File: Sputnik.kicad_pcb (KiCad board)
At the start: 4 copper layers, 130 x 65 mm, 179 parts, among them IC1 EP4CE10F17, J1 Pinheader_2x5_TH_WALL, P1 USB_A, U1 SN74LVC2T45, U10 SN74LVC8T245, U11 SN74LVC8T245, U12 SN74LVC8T245, U13 SN74LVC8T245, U14 SN74LVC8T245, U15 SN74LVC8T245, U16 SN74LVC2T45, U17 SN74LVC2T45, U18 SN74LVC2T45, U19 SN74LVC1G07DCK, U2 SN74LVC2T45, U20 SN74LVC2T45, U21 EPCS4, U22 W9751G6KB, U23 FT313HL-LQFP64-0.5, U24 TLV62569P, U25 TPS2024D, U3 SN74LVC1G07DCK, U4 SN74LVC2T45, U5 DM9000B, U6 93LC46, U7 74LVC2G07, U8 Pulse-J00-0045NL, U9 SN74LVC8T245, X2 Zorro_Connector, Y1 25MHz, Y2 12MHz

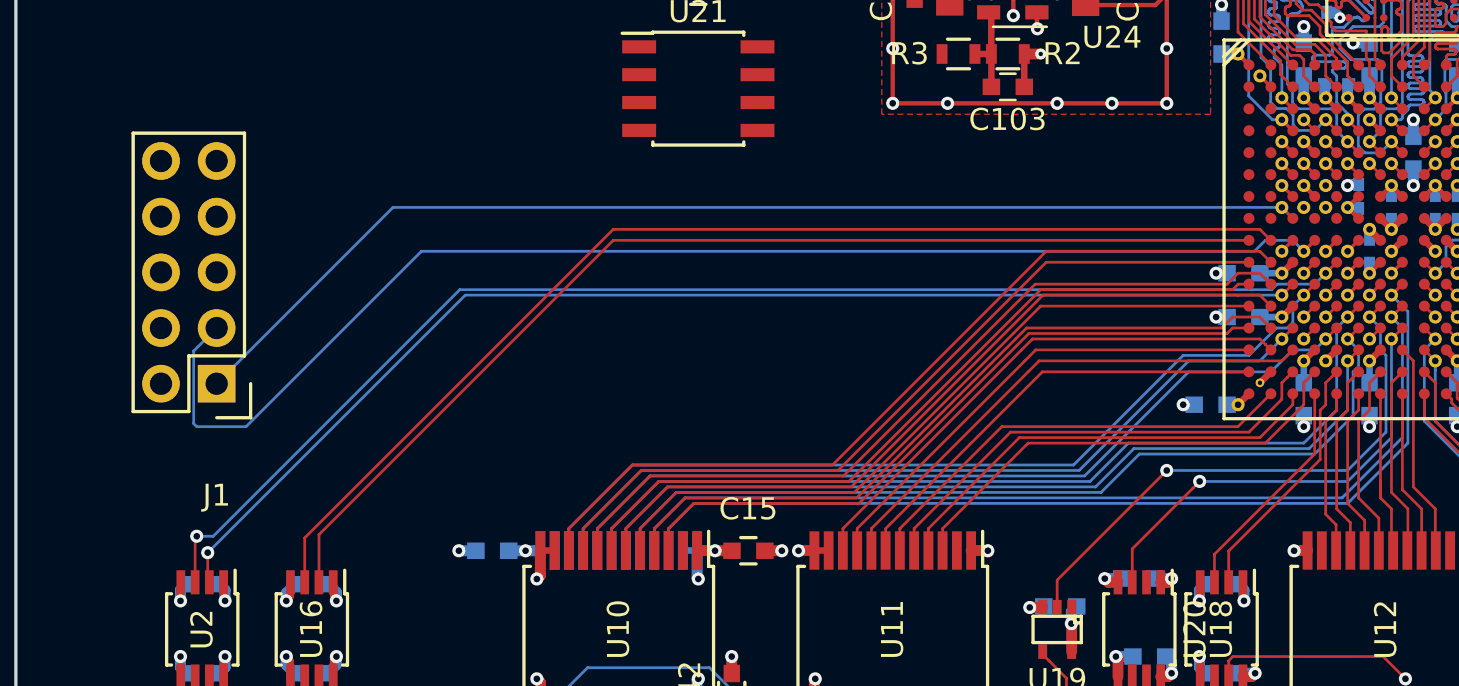
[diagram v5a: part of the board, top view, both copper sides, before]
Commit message: PCB rework, JTAG connector moved, VREF routed
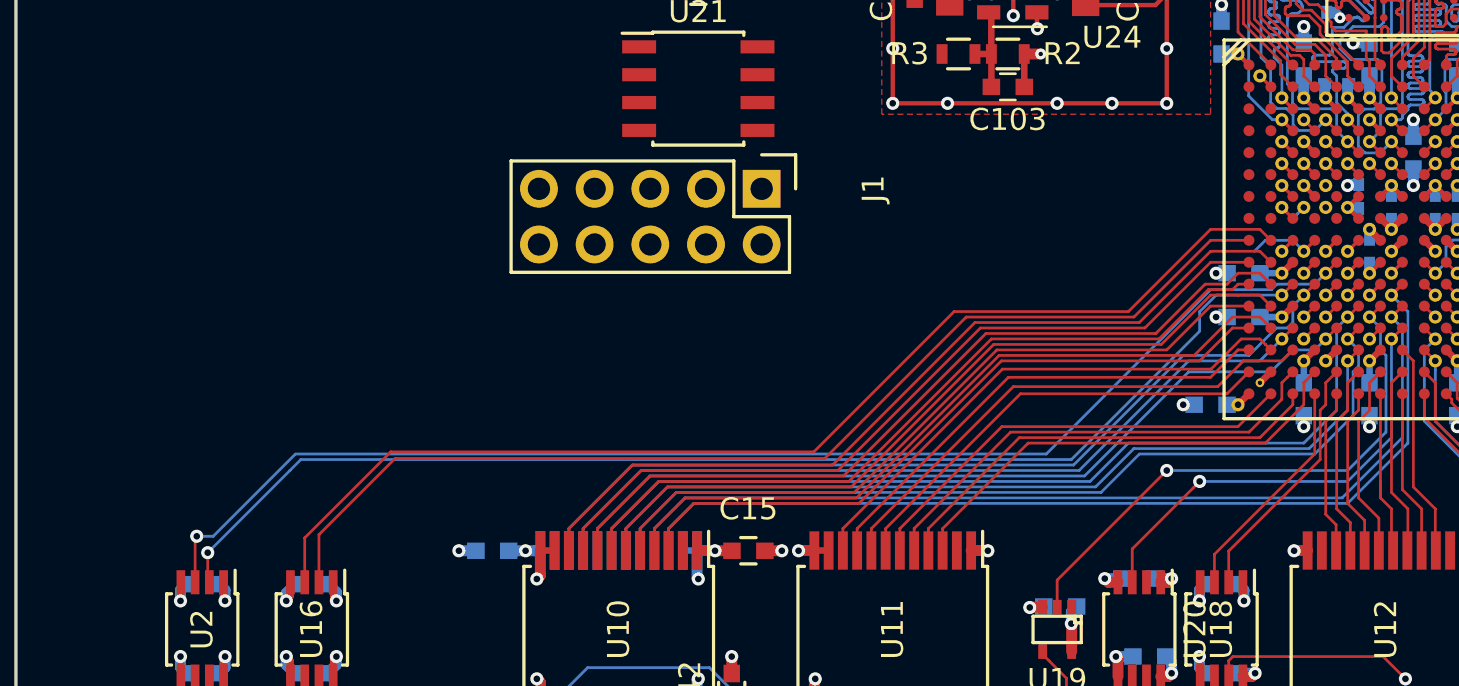
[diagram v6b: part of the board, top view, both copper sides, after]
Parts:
- moved J1 26.4 mm to (154.0, 41.4), turned to 270 degrees
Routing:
- net /fpga/TDO: track 59.9 -> 3.37 mm
- net /fpga/TCK: track 52.6 -> 0.71 mm
- net /RAM/VREF: track 20.4 -> 26.6 mm
- net (no net): track 0.00 -> 1.25 mm, vias 0 -> 4
- net +5VDC: track 117.7 -> 116.5 mm, vias 25 -> 21
- net /fpga/TDI: track 0.00 -> 0.69 mm
- net /Zorro/nIORST: track 56.0 -> 56.5 mm

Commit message: Up
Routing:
- net /fpga/TDO: track 3.37 -> 15.7 mm
- net /fpga/TMS: track 0.71 -> 9.27 mm
- net /fpga/TDI: track 0.69 -> 7.96 mm
- net /fpga/TCK: track 0.71 -> 7.27 mm
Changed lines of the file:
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@@
     (thickness 1.6)
     (drawings 9)
-    (tracks 7427)
+    (tracks 7436)
     (zones 0)
     (modules 179)
@@
   (segment (start 178.2509 40.75064) (end 178.25064 40.75064) (width 0.15) (layer F.Cu) (net 148))
   (segment (start 178.25064 40.75064) (end 177.75 40.25) (width 0.15) (layer F.Cu) (net 148))
+  (segment (start 177 43) (end 171.5 43) (width 0.125) (layer B.Cu) (net 150))
+  (segment (start 177.450001 42.549999) (end 177 43) (width 0.125) (layer B.Cu) (net 150))
+  (segment (start 177.75 42.25) (end 177.450001 42.549999) (width 0.125) (layer B.Cu) (net 150))
   (segment (start 178.2509 42.74962) (end 178.24962 42.74962) (width 0.15) (layer F.Cu) (net 150))
   (segment (start 178.24962 42.74962) (end 177.75 42.25) (width 0.15) (layer F.Cu) (net 150))
-  (segment (start 178.450001 42.549999) (end 178.262499 42.737501) (width 0.125) (layer B.Cu) (net 151))
-  (segment (start 178.75 42.25) (end 178.450001 42.549999) (width 0.125) (layer B.Cu) (net 151))
+  (segment (start 178.25 43.25) (end 171.5 43.25) (width 0.125) (layer B.Cu) (net 151))
+  (segment (start 178.75 42.75) (end 178.25 43.25) (width 0.125) (layer B.Cu) (net 151))
+  (segment (start 178.75 42.25) (end 178.75 42.75) (width 0.125) (layer B.Cu) (net 151))
+  (segment (start 178.25 43.75) (end 171.5 43.75) (width 0.125) (layer B.Cu) (net 152))
   (segment (start 178.75 44.25) (end 178.25 43.75) (width 0.125) (layer B.Cu) (net 152))
-  (segment (start 178.25 43.75) (end 177 43.75) (width 0.125) (layer B.Cu) (net 152))
-  (segment (start 177 43.75) (end 176.5 44.25) (width 0.125) (layer B.Cu) (net 152))
+  (segment (start 177.087501 44.5) (end 171.5 44.5) (width 0.125) (layer B.Cu) (net 152))
+  (segment (start 178.75 44.25) (end 178.25 44.75) (width 0.125) (layer B.Cu) (net 152))
+  (segment (start 178.25 44.75) (end 177.337501 44.75) (width 0.125) (layer B.Cu) (net 152))
+  (segment (start 177.337501 44.75) (end 177.087501 44.5) (width 0.125) (layer B.Cu) (net 152))
   (segment (start 179.24912 43.75038) (end 179.24912 43.75088) (width 0.15) (layer F.Cu) (net 152))
   (segment (start 179.24912 43.75088) (end 178.75 44.25) (width 0.15) (layer F.Cu) (net 152))
@@
   (segment (start 179.24912 53.50088) (end 179.24912 52.75088) (width 0.125) (layer F.Cu) (net 175))
   (segment (start 179.24912 52.75088) (end 179.24912 50.75062) (width 0.125) (layer F.Cu) (net 175))
+  (segment (start 179 43.5) (end 171.5 43.5) (width 0.125) (layer B.Cu) (net 177))
+  (segment (start 179.75 44.25) (end 179 43.5) (width 0.125) (layer B.Cu) (net 177))
   (segment (start 179.75 44.25) (end 179.75026 44.25) (width 0.15) (layer F.Cu) (net 177))
   (segment (start 179.75026 44.25) (end 180.24988 43.75038) (width 0.15) (layer F.Cu) (net 177))
@@
     (polygon
       (pts
-        (xy 182.25 41.75) (xy 182.25 40.5) (xy 186.25 40.5) (xy 186.25 43.75) (xy 184.5 43.75)
-        (xy 183.75 44.5) (xy 183.75 46) (xy 180 46) (xy 180 43.75) (xy 168 43.75)
-        (xy 168 42.75) (xy 180 42.75) (xy 180 41.75)
+        (xy 180.25 40.5) (xy 182.25 40.5) (xy 186.25 40.5) (xy 186.25 43.75) (xy 184.5 43.75)
+        (xy 183.75 44.5) (xy 183.75 45.75) (xy 180 45.75) (xy 180 43.75) (xy 168 43.75)
+        (xy 168 42.75) (xy 168 40.5) (xy 178.25 40.5)
       )
     )

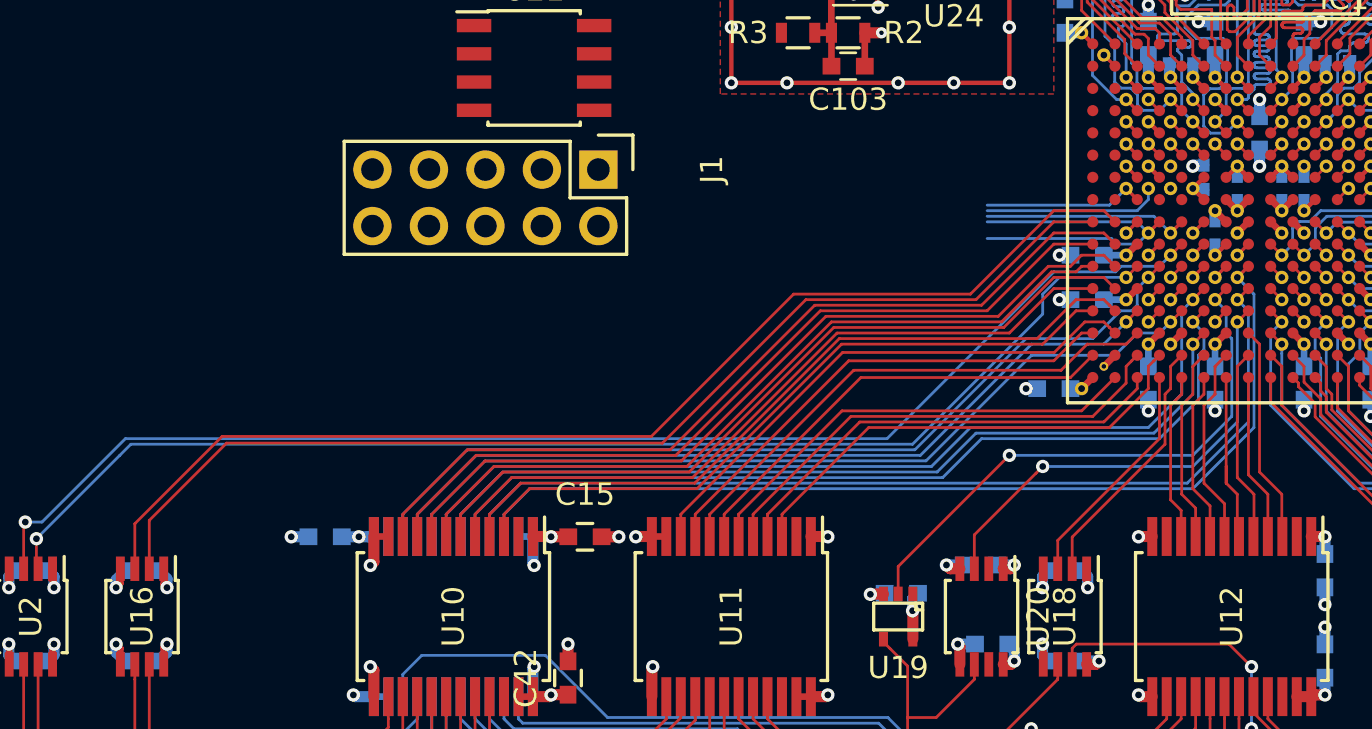
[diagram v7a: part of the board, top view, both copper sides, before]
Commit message: Top tracks cleanup
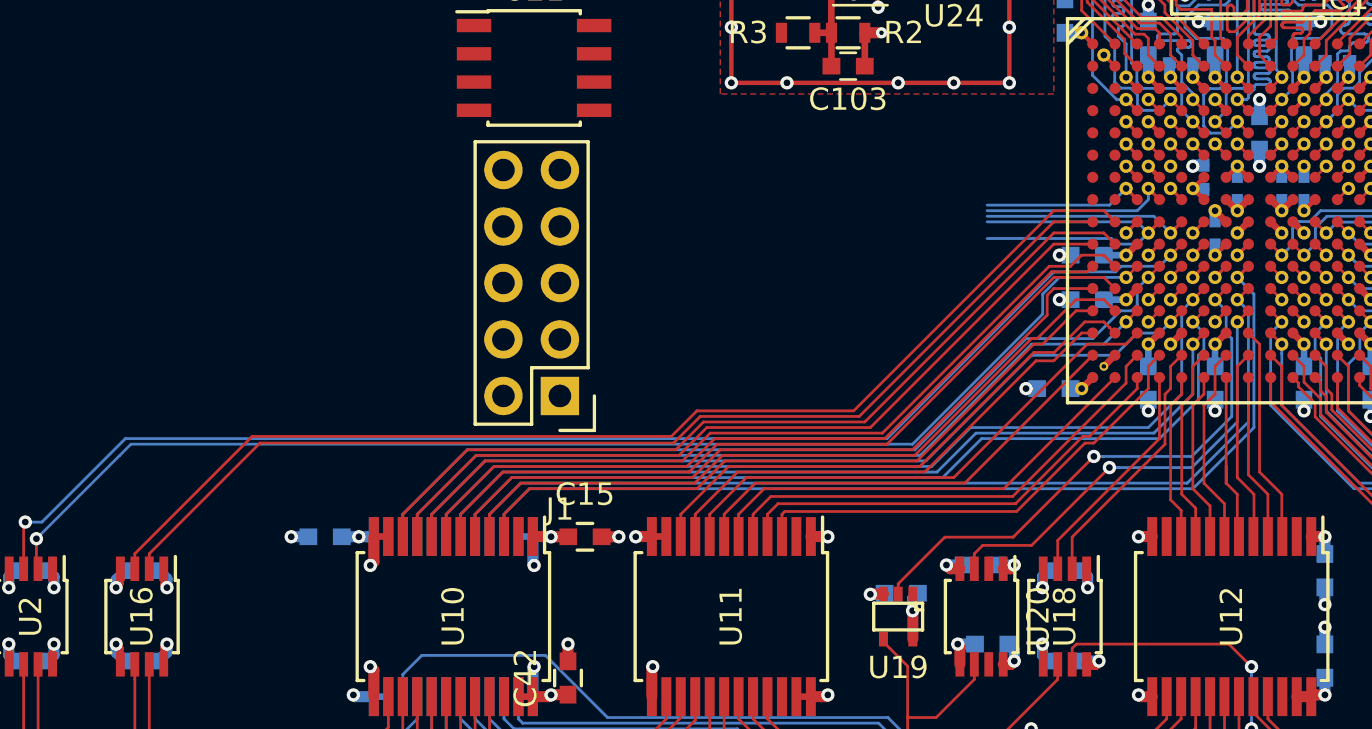
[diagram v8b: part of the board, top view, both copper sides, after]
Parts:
- moved J1 10.3 mm to (152.3, 51.6), turned to 180 degrees
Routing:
- net /fpga/SenseZ3: track 50.2 -> 49.3 mm
- net /Zorro/7M_: track 52.1 -> 51.3 mm
- net /fpga/nCONFIG: track 0.00 -> 0.71 mm
- net /fpga/TDI: track 7.96 -> 8.66 mm
- net /Zorro/SD_2: track 33.0 -> 33.5 mm
